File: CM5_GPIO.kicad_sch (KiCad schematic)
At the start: 34 parts, among them J14 JST_SHBM04B-SRSS-TB, J2 Conn_02x07_Odd_Even, J3 Conn_01x03, J7 Micro_SD_Card_Det, J8 THD-20-R, J9 THD-02-R, SW1 Right angle Tact button, U1 TPD4EUSB30, U18 RT9742GGJ5, U2 TPD4EUSB30, U3 MagJack-A70-112-331N126

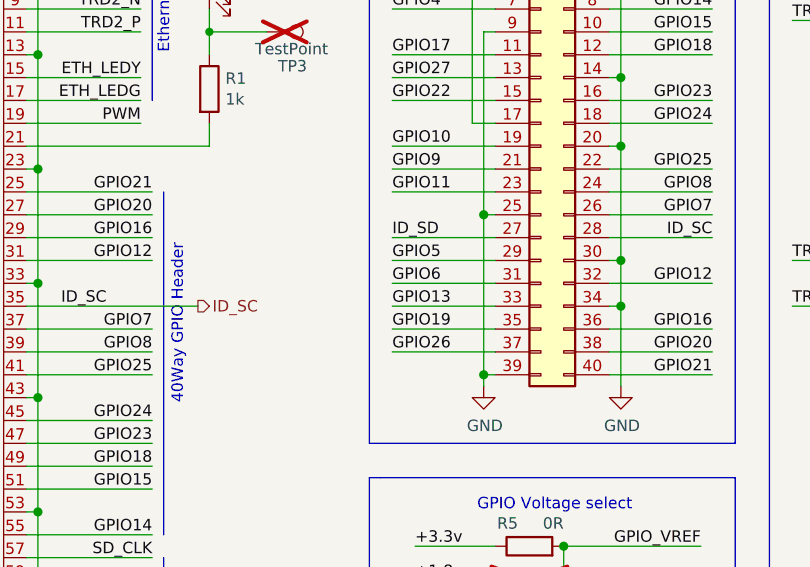
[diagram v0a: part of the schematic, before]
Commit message: Added level shifter
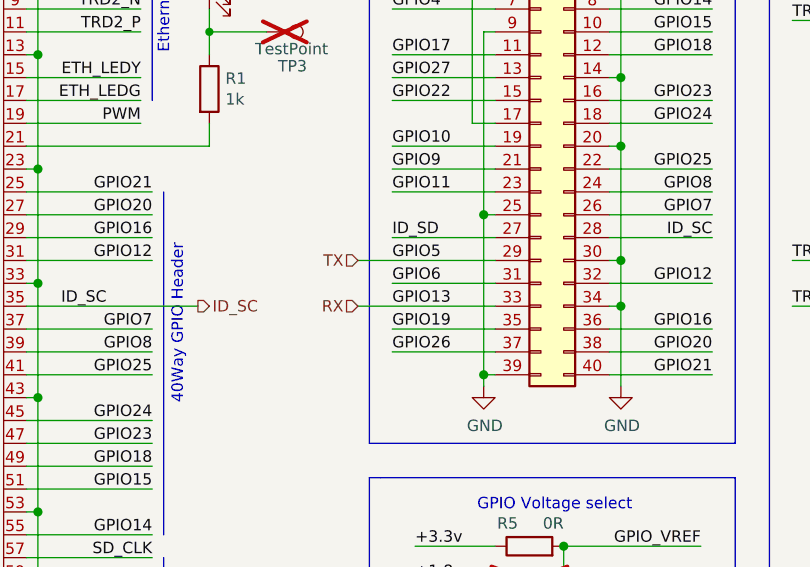
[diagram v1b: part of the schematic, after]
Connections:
- net GPIO13 renamed RX
- net GPIO5 renamed TX
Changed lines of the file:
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@@
 	(wire
 		(pts
-			(xy 140.97 59.69) (xy 152.4 59.69)
+			(xy 137.16 59.69) (xy 152.4 59.69)
 		)
 		(stroke
@@
 	(wire
 		(pts
-			(xy 140.97 64.77) (xy 152.4 64.77)
+			(xy 137.16 64.77) (xy 152.4 64.77)
 		)
 		(stroke
@@
 		)
 	)
+	(hierarchical_label "TX"
+		(shape input)
+		(at 137.16 59.69 180)
+		(effects
+			(font
+				(size 1.27 1.27)
+			)
+			(justify right)
+		)
+	)
 	(hierarchical_label "CAM_GPIO0"
 		(shape output)
@@
 		)
 	)
+	(hierarchical_label "RX"
+		(shape input)
+		(at 137.16 64.77 180)
+		(effects
+			(font
+				(size 1.27 1.27)
+			)
+			(justify right)
+		)
+	)

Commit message: Need to fix ERC
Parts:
- removed BT1: Battery_Cell, CM5IO:BatteryHolder_Keystone_3034_1x20mm, symbol Device:Battery_Cell
- removed C5: 10u, Capacitor_SMD:C_0805_2012Metric, symbol Device:C
- removed J14: JST_SHBM04B-SRSS-TB, Connector_JST:JST_SH_BM04B-SRSS-TB_1x04-1MP_P1.00mm_Vertical, symbol Connector_Generic:Conn_01x04
- removed J2: Conn_02x07_Odd_Even, Connector_PinHeader_2.54mm:PinHeader_2x07_P2.54mm_Vertical, symbol Connector_Generic:Conn_02x07_Odd_Even
- removed J3: Conn_01x03, Connector_PinHeader_2.54mm:PinHeader_1x03_P2.54mm_Vertical, symbol Connector_Generic:Conn_01x03
- removed J7: Micro_SD_Card_Det, CM5IO:SDCARD_MOLEX_503398-1892, symbol Connector:Micro_SD_Card_Det2
- removed J9: THD-02-R, Connector_PinHeader_2.54mm:PinHeader_2x02_P2.54mm_Vertical, symbol Connector_Generic:Conn_02x02_Odd_Even
- removed R18, R19, R20, R21, R22: 0R, Resistor_SMD:R_0603_1608Metric_Pad0.98x0.95mm_HandSolder, symbol Device:R
- removed R4: 0R, Resistor_SMD:R_0805_2012Metric_Pad1.20x1.40mm_HandSolder, symbol Device:R
- removed TP4: TestPoint, TestPoint:TestPoint_Pad_2.0x2.0mm, symbol Connector:TestPoint
- removed U1, U2: TPD4EUSB30, Package_SON:USON-10_2.5x1.0mm_P0.5mm, symbol CM5IO:TPD4EUSB30
- removed U18: RT9742GGJ5, Package_TO_SOT_SMD:SOT-23-5, symbol CM5IO:RT9742GGJ5
- added JP3, JP6: SolderJumper_2_Open, symbol Jumper:SolderJumper_2_Open
- added JP4, JP5: SolderJumper_2_Open, Jumper:SolderJumper-2_P1.3mm_Open_RoundedPad1.0x1.5mm, symbol Jumper:SolderJumper_2_Open
- added Q1, Q2: FDV301N, FDV301N:SOT23, symbol FDV301N:FDV301N
- added R10, R7, R8, R9: 4K7, Resistor_SMD:R_0603_1608Metric_Pad0.98x0.95mm_HandSolder, symbol Device:R
- added R12, R14: R, Resistor_SMD:R_0603_1608Metric_Pad0.98x0.95mm_HandSolder, symbol Device:R
- added TP1: TestPoint, TestPoint:TestPoint_Pad_2.0x2.0mm, symbol Connector:TestPoint
- added U2, U3: 74LVC1G17, Package_TO_SOT_SMD:SOT-23-5_HandSoldering, symbol 74xGxx:74LVC1G17
- R11: value 10K 1% -> R; footprint Resistor_SMD:R_0402_1005Metric -> Resistor_SMD:R_0603_1608Metric_Pad0.98x0.95mm_HandSolder; Field4 Farnell -> (none); Field6 MCR01MZPF1002 -> (none); Field7 Rohm -> (none); Part Description Resistor 10K M1005 1% 63mW -> (none)
- R13: value 10K 1% -> R; footprint Resistor_SMD:R_0402_1005Metric -> Resistor_SMD:R_0603_1608Metric_Pad0.98x0.95mm_HandSolder; Field4 Farnell -> (none); Field6 MCR01MZPF1002 -> (none); Field7 Rohm -> (none); Part Description Resistor 10K M1005 1% 63mW -> (none); now fitted; now in the parts list
- renumbered C1 to C7, D2 to D1, D1 to D2, J8 to J5, R1 to R15, R10 to R16, R2 to R17, R3 to R18, R5 to R6, TP5 to TP3, TP3 to TP4, U3 to U4
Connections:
- net +3.3v: now also Q1.1, Q2.1, R10.1, R9.1, U2.5 (VCC), U3.5 (VCC); no longer R11.1, R13.1
- net +5v: now also R7.1, R8.1
- net BT_nDis: now also R12.1
- net EEPROM_nWP: now also R13.1
- net GND: now also R11.2, R13.2, JP3.2 (B), JP6.2 (B), R12.2, R14.2, U2.3 (GND), U3.3 (GND)
- net GPIO15: now also U3.4
- net PMIC_ENABLE: now also JP6.1 (A)
- net USBOTG: now also JP3.1 (A)
- net WL_nDis: now also R11.1
- net nRPIBOOT: now also R14.1
- net Activity_LED: now reaches Module1.21 (LED_nACT), R15.2
- removed net PWM: Module1.19 (FAN_PWM), R11.2, TP2.1
- net RX renamed GPIO13
- net GPIO13: now also U2.4
- net SD_CLK: no longer names the net of Module1.57 (SD_CLK)
- net SD_CMD: no longer names the net of Module1.62 (SD_CMD)
- net SD_DAT0: no longer names the net of Module1.63 (SD_DAT0)
- net SD_DAT1: no longer names the net of Module1.67 (SD_DAT1)
- net SD_DAT2: no longer names the net of Module1.69 (SD_DAT2)
- net SD_DAT3: no longer names the net of Module1.61 (SD_DAT3)
- net SD_PWR_ON: no longer names the net of Module1.75 (SD_PWR_ON)
- net SD_PWR_ON: no longer R13.2
- net SYNC_OUT: no longer names the net of Module1.18 (Ethernet_SYNC_OUT(3.3v))
- net TACHO: no longer names the net of Module1.16 (FAN_TACHO)
- net TR0_TAP: no longer names the net of U4.11 (VC1)
- net TR1_TAP: no longer names the net of U4.12 (VC2)
- net TR2_TAP: no longer names the net of U4.13 (VC3)
- net TR3_TAP: no longer names the net of U4.14 (VC4)
- net TX renamed GPIO5
- new net: JP5.2 (B), Q2.2, R10.2, U2.2
- new net: JP4.2 (B), Q1.2, R9.2, U3.2
- new net DeviceRX: JP4.1 (A), Q1.3, R7.2, TP1.1
- new net DeviceTX: JP5.1 (A), Q2.3, R8.2, TP2.1
- no-connect marks 9 -> 19
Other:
- note added: "5v to 3.3v level translator"
- note added: "Feedback"
- note added: "Options"
- note removed: "CM5Lite SDCARD I/F"
- note removed: "Ethernet POE Protection"
- note removed: "FAN connector"
- note removed: "Force RPIBOOT = Jumper Pins 1-2"
- note removed: "Not Fitted header"
- note removed: "POE Header"
- note removed: "R2 : Add R13 to support CM4Lite"
- note removed: "R2 : Pullup added for Fans that don't have a strong internal pullup"
- note removed: "R2 : Simplify nPWR_LED Drive"
- moved on the sheet: D1, D2, J5, R15, R16, R6, SW1, TP3, TP4

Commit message: schematic review
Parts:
- removed JP4, JP5: SolderJumper_2_Open, Jumper:SolderJumper-2_P1.3mm_Open_RoundedPad1.0x1.5mm, symbol Jumper:SolderJumper_2_Open
- removed Q1, Q2: FDV301N, FDV301N:SOT23, symbol FDV301N:FDV301N
- removed R10, R7, R8, R9: 4K7, Resistor_SMD:R_0603_1608Metric_Pad0.98x0.95mm_HandSolder, symbol Device:R
- removed TP1, TP2: TestPoint, TestPoint:TestPoint_Pad_2.0x2.0mm, symbol Connector:TestPoint
- removed U2, U3: 74LVC1G17, Package_TO_SOT_SMD:SOT-23-5_HandSoldering, symbol 74xGxx:74LVC1G17
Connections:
- net GPIO13 renamed TX
- net GPIO15 renamed RX
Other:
- note removed: "5v to 3.3v level translator"
- note removed: "Feedback"
- company: Copyright © 2024 Raspberry Pi Ltd. -> Astrosystems
- title: Compute Module 5 IO Board - GPIO - Ethernet -> CM4/5 GPIO + Ethernet
- moved on the sheet: D1, D2, J5, JP3, JP6, R11, R12, R13, R14, R15, R16, R6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

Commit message: updated files
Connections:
- net VBAT: no longer names the net of Module1.76 (VBAT)
- no-connect marks 19 -> 20
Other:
- note added: "GPIO13"
- note added: "GPIO15"
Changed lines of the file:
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@@
 		)
 	)
+	(text "GPIO13"
+		(exclude_from_sim no)
+		(at 161.036 71.374 0)
+		(effects
+			(font
+				(size 1.27 1.27)
+			)
+		)
+	)
+	(text "GPIO13"
+		(exclude_from_sim no)
+		(at 27.686 53.848 0)
+		(effects
+			(font
+				(size 1.27 1.27)
+			)
+		)
+	)
+	(text "GPIO15"
+		(exclude_from_sim no)
+		(at 189.484 40.894 0)
+		(effects
+			(font
+				(size 1.27 1.27)
+			)
+		)
+	)
 	(text "GPIO Voltage select\n"
 		(exclude_from_sim no)
@@
 		)
 	)
+	(text "GPIO15"
+		(exclude_from_sim no)
+		(at 110.744 84.328 0)
+		(effects
+			(font
+				(size 1.27 1.27)
+			)
+		)
+	)
 	(text "PWR LED"
 		(exclude_from_sim no)
@@
 	)
 	(no_connect
+		(at 39.37 115.57)
+	)
+	(no_connect
 		(at 39.37 110.49)
 	)
@@
 		)
 	)
-	(wire
-		(pts
-			(xy 25.4 115.57) (xy 39.37 115.57)
-		)
-		(stroke
-			(width 0)
-			(type solid)
-		)
-	)
 	(polyline
 		(pts
@@
 	(wire
 		(pts
-			(xy 24.13 54.61) (xy 39.37 54.61)
-		)
-		(stroke
-			(width 0)
-			(type solid)
-		)
-	)
-	(wire
-		(pts
 			(xy 100.33 52.07) (xy 114.3 52.07)
 		)
@@
 	(wire
 		(pts
-			(xy 100.33 85.09) (xy 114.3 85.09)
+			(xy 100.33 85.09) (xy 116.84 85.09)
 		)
 		(stroke
@@
 	(wire
 		(pts
+			(xy 20.32 54.61) (xy 39.37 54.61)
+		)
+		(stroke
+			(width 0)
+			(type default)
+		)
+	)
+	(wire
+		(pts
 			(xy 38.1 21.59) (xy 38.1 29.21)
 		)
@@
 		)
 	)
-	(label "GPIO15"
-		(at 114.3 85.09 180)
-		(effects
-			(font
-				(size 1.27 1.27)
-			)
-			(justify right bottom)
-		)
-	)
-	(label "GPIO13"
-		(at 24.13 54.61 0)
-		(effects
-			(font
-				(size 1.27 1.27)
-			)
-			(justify left bottom)
-		)
-	)
 	(label "GPIO7"
 		(at 114.3 67.31 180)
@@
 		)
 	)
-	(label "GPIO15"
-		(at 193.04 41.91 180)
-		(effects
-			(font
-				(size 1.27 1.27)
-			)
-			(justify right bottom)
-		)
-	)
 	(label "GPIO5"
 		(at 157.48 67.31 0)
@@
 		)
 	)
-	(label "VBAT"
-		(at 25.4 115.57 0)
-		(effects
-			(font
-				(size 1.27 1.27)
-			)
-			(justify left bottom)
-		)
-	)
 	(label "ID_SC"
 		(at 114.3 64.77 180)
@@
 		)
 	)
-	(label "GPIO13"
-		(at 157.48 72.39 0)
-		(effects
-			(font
-				(size 1.27 1.27)
-			)
-			(justify left bottom)
-		)
-	)
 	(label "GPIO_VREF"
 		(at 279.4 110.49 180)
@@
 		)
 	)
+	(hierarchical_label "TX"
+		(shape input)
+		(at 20.32 54.61 180)
+		(effects
+			(font
+				(size 1.27 1.27)
+			)
+			(justify right)
+		)
+	)
 	(hierarchical_label "+3.3v"
 		(shape output)
@@
 		(effects
 			(font
+				(size 1.27 1.27)
+			)
+			(justify left)
+		)
+	)
+	(hierarchical_label "RX"
+		(shape input)
+		(at 116.84 85.09 0)
+		(effects
+			(font
